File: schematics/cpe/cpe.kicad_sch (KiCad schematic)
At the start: 54 parts

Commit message: further CPE schematic updates
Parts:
- removed U24: ~, symbol peppercorn:CONFIG
- added C10, C11, C12, C13, C14, C15, C16, C17, C8, C9: ~, symbol peppercorn:MUX2B
- added FF1, FF2: ~, symbol peppercorn:DFF
- added L28: ~, symbol peppercorn:LUT2
- added L29, L30, L31, L32: ~, symbol peppercorn:LUT1
- added LT1, LT2: ~, symbol peppercorn:DLT
- added M16: ~, symbol peppercorn:MUX4 (conceptual) (upside down)
- added M17, M18, M19: ~, symbol peppercorn:MUX4
- added U24, U67, U8, U82, U83, U9: ~, symbol peppercorn:AND
- added U35, U37, U45, U80, U81, U92, U93, U96, U97, U98, U99: ~, symbol peppercorn:CONFIG
- added U77, U79, U87, U88: ~, symbol peppercorn:XOR
- added U89, U90, U91, U94, U95: ~, symbol peppercorn:NOT
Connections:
- net CINY1: now also U67., U83.
- net CLK: now also FF1.C, FF2.C, L31.D, LT1.G, LT2.G, U88.
- net COMB1OUT: now also L28.D0, M17.D0, M18.D3, U89.
- net COMB2OUT: now also L28.D1, M17.D1, M19.D3
- net EN: now also C9.D0, FF1.E, FF2.E, L30.D, LT1.E, LT2.E, U87.
- net MUXOUT: now also M17.D2, M18.D1, M19.D1, U91.
- net PINY1: now also U24., U82.
- net SR: now also C9.D1, L29.D
- net at C4.D1: now also U15.B, U19.
- net at U18.B, U21.: now also C2.D1
- net at U23.: now also U24.; no longer C3.D1
- net at U17.A: now also U79.; no longer L6.Y
- net at U17.B, U20.: now also C3.D1
- net at U22.: now also U67.; no longer C2.D1
- net at L7.Y: now also U77.; no longer U15.A
- new net: U81., U83.
- new net: U13., U5.
- new net: M19.D0, U95.
- new net: C15.Y, M19.D2
- new net: M19.S0, U98.
- new net: M19.S1, U99.
- new net: C17.D1, M19.Y, U9.
- new net: M10.D0, U27., U28.
- new net: M18.D0, U94.
- new net: C14.Y, M18.D2
- new net: M18.S0, U96.
- new net: M18.S1, U97.
- new net: C16.D1, M18.Y, U8.
- new net: M16.S0, U45.
- new net: U35., U8.
- new net: M11.S, U31., U32., U34.
- new net: U82., U87.
- new net: U80., U82.
- new net: U67., U77.
- new net: U24., U79.
- new net: C9.Y, L32.D
- new net: C8.Y, M16.D3
- new net: L30.Y, U87.
- new net: M10.S, U27., U32., U33.
- new net: U26., U27., U30.
- new net: U15.A, U77.
- new net: L31.Y, U88.
- new net: M17.D3, U91.
- new net: M17.S0, U92.
- new net: M17.S1, U93.
- new net: M17.Y, U90.
- new net: U37., U9.
- new net: C13.Y, C14.D1, C15.D0
- new net: C12.Y, C14.D0, C15.D1
- new net: L6.Y, U79.
- new net: C10.D0, FF2.Q
- new net: C10.D1, LT2.Q
- new net: C10.Y, U95.
- new net: U83., U88.
- new net: FF1.D, LT1.D, U89.
- new net: FF2.D, LT2.D, U90.
- new net: C11.D0, FF1.Q
- new net: C11.Y, U94.
- new net: C11.D1, LT1.Q
- new net COMPOUT: L28.Y
- new net COUTX: C13.D1
- new net COUTY1: C13.D0
- new net OUT1: C16.Y
- new net OUT2: C17.Y
- new net POUTX: C12.D1
- new net POUTY1: C12.D0
- new net RAM_I1: C16.D0
- new net RAM_I2: C17.D0
- new net RAM_O1: U8.
- new net RAM_O2: U9.
- new net RST: FF1.S, FF2.S, L29.Y, LT1.S, LT2.S
- new net SET: FF1.R, FF2.R, L32.Y, LT1.R, LT2.R
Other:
- sheet C_FUNCTION=0 renamed C_FUNCTION=0 or 6
- sheet C_FUNCTION=1 renamed C_FUNCTION=1 or 7
- removed sheet C_FUNCTION=6
- added sheet C_FUNCTION=2 or 3 (cpe_comb_addf2.kicad_sch)
- sheet C_FUNCTION=1 or 7: file cpe_comb_addf.kicad_sch -> cpe_comb_addcin.kicad_sch
- note added: "COMBINATIONAL LOGIC"
- note added: "C_CLKSEL"
- note added: "C_C_P"
- note added: "C_ENSEL"
- note added: "C_EN_SR"
- note added: "C_HMULT"
- note added: "C_L_D"
- note added: "C_O1[0]"
- note added: "C_O1[1]"
- note added: "C_O2[0]"
- note added: "C_O2[1]"
- note added: "C_RAMI1"
- note added: "C_RAMI2"
- note added: "C_RAM_O1"
- note added: "C_RAM_O2"
- note added: "C_S"
- note added: "C_SELX"
- note added: "C_Y12"
- note added: "D FLIP FLOP"
- note added: "D LATCH"
- note added: "SEQUENTIAL LOGIC"
- company: (none) -> YosysHQ

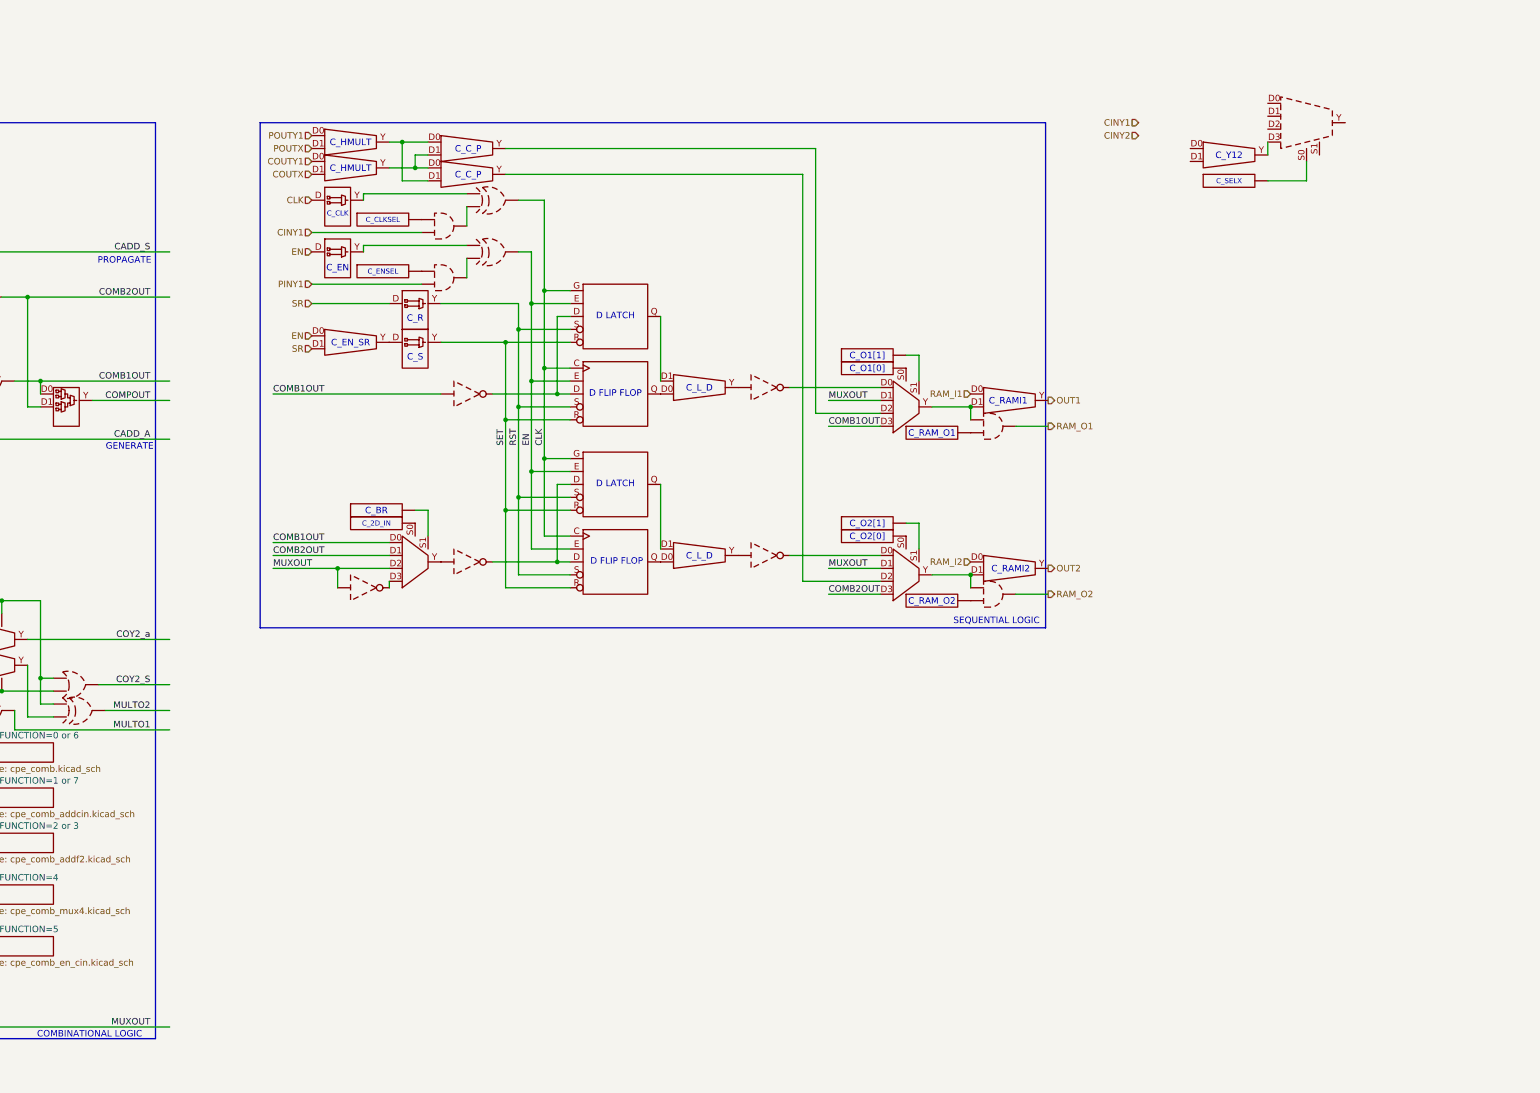
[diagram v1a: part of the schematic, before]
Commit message: update CPE schematics to cover C/P lines
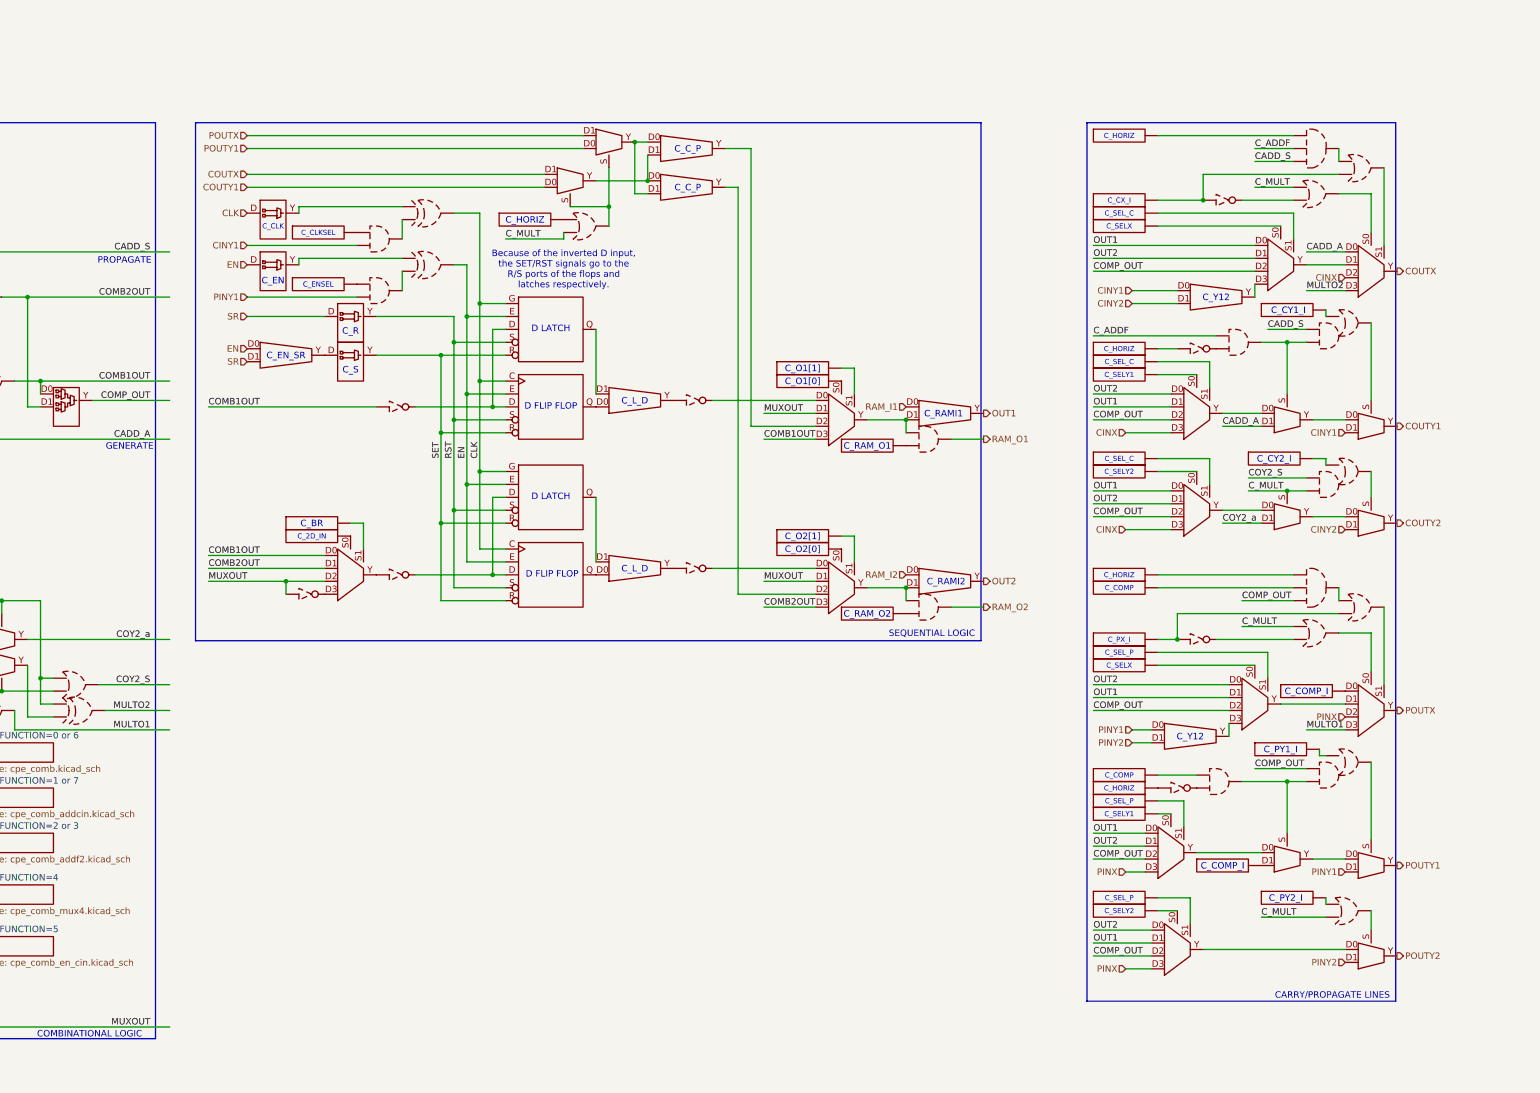
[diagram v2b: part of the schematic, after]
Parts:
- removed C13: ~, symbol peppercorn:MUX2B
- removed M16: ~, symbol peppercorn:MUX4 (conceptual) (upside down)
- added M16, M22, M27, M32, M33, M34, M37, M39: ~, symbol peppercorn:MUX4
- added M23, M24, M25, M26, M28, M29, M35, M36, M38: ~, symbol peppercorn:MUX2
- added U100, U101, U103, U107, U108, U109, U110, U111, U112, U115, U117, U119, U120, U121, U40, U51, U62, U63, U68, U69, U72, U73, U76, U78, U85, U86: ~, symbol peppercorn:CONFIG
- added U102, U105, U118, U44, U55, U60: ~, symbol peppercorn:OR
- added U104, U113, U50, U74: ~, symbol peppercorn:NOT
- added U106, U57: ~, symbol peppercorn:AND3
- added U114, U75: ~, symbol peppercorn:AND
- added U116, U70, U84: ~, symbol peppercorn:OA21
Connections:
- net CADD_A: now also M22.D0, M25.D1
- net CADD_S: now also U57., U70.
- net CINX: now also M22.D2, M27.D3, M32.D3
- net CINY1: now also C8.D0, M26.D1
- net CINY2: now also C8.D1, M29.D1
- net COUTX: now also M22.Y, M23.D1
- net COUTY1: now also M23.D0, M26.Y
- net COY2_S: now also U84.
- net COY2_a: now also M28.D1
- net MULTO1: now also M33.D3
- net MULTO2: now also M22.D3
- net OUT1: now also M16.D0, M27.D1, M32.D0, M34.D1, M37.D0, M39.D1
- net OUT2: now also M16.D1, M27.D0, M32.D1, M34.D0, M37.D1, M39.D0
- net PINX: now also M33.D2, M37.D3, M39.D3
- net PINY1: now also C12.D0, M35.D1
- net PINY2: now also C12.D1, M38.D1
- net POUTX: now also M24.D1, M33.Y; no longer C12.D1
- net POUTY1: now also M24.D0, M35.Y; no longer C12.D0
- net at U45.: now also M16.S0
- net at U77.: now also U15.A; no longer U67.
- net at U79.: now also L6.Y; no longer U24.
- net at C8.Y: now also M16.D3
- net at C14.D1, C15.D0: now also M23.Y
- net at C14.D0, C15.D1: now also M24.Y; no longer C12.Y
- net COMPOUT renamed COMP_OUT
- net COMP_OUT: now also M16.D2, M27.D2, M32.D2, M34.D2, M37.D2, M39.D2, U106., U116.
- new net: M33.D0, U86.
- new net: U13., U5.
- new net: M37.S0, U112.
- new net: M28.Y, M29.D0
- new net: M29.S, U84.
- new net: M10.D0, U27., U28.
- new net: U106., U107.
- new net: U118., U119.
- new net: M38.S, U118.
- new net: U84., U85.
- new net: U103., U104., U105.
- new net: U102., U104.
- new net: M23.S, M24.S, U60.
- new net: M36.S, U114., U116.
- new net: U114., U115.
- new net: U113., U114.
- new net: M16.S1, U40.
- new net: M28.D0, M32.Y
- new net: M27.S1, U68.
- new net: M34.S0, U101.
- new net: M25.S, U70., U75.
- new net: U74., U75.
- new net: M33.S1, U105.
- new net: U105., U106.
- new net: M11.S, U31., U32., U34.
- new net: U82., U87.
- new net: U67., U77.
- new net: M39.S1, U120.
- new net: U44., U50.
- new net: M22.S0, U44.
- new net: U110., U113.
- new net: U24., U79.
- new net: M38.D0, M39.Y
- new net: U60., U63.
- new net: M26.S, U70.
- new net: U70., U72.
- new net: M36.D1, U109.
- new net: M10.S, U27., U32., U33.
- new net: U26., U27., U30.
- new net: U73., U74.
- new net: M32.S0, U78.
- new net: M32.S1, U76.
- new net: M33.D1, M34.Y
- new net: M33.S0, U102.
- new net: U116., U117.
- new net: M35.S, U116.
- new net: M37.S1, U111.
- new net: M36.D0, M37.Y
- new net: M34.S1, U100.
- new net: M39.S0, U121.
- new net: U50., U51., U55.
- new net: U57., U62.
- new net: M16.Y, M22.D1
- new net: C12.Y, M34.D3
- new net: M35.D0, M36.Y
- new net: M22.S1, U55.
- new net: M27.S0, U69.
- new net: M25.D0, M27.Y
- new net: U83., U88.
- new net: M25.Y, M26.D0
- new net: U106., U108.
- new net: U55., U57.
- new net COUTY2: M29.Y
- new net C_ADDF: U57., U75.
- new net C_MULT: M28.S, U102., U118., U44., U60., U84.
- new net POUTY2: M38.Y
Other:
- note added: "Because of the inverted D input, the SET/RST signals go to the R/S ports of the flops and latches respectively."
- note added: "CARRY/PROPAGATE LINES"
- note added: "C_COMP"
- note added: "C_COMP_I"
- note added: "C_CX_I"
- note added: "C_CY1_I"
- note added: "C_CY2_I"
- note added: "C_PX_I"
- note added: "C_PY1_I"
- note added: "C_PY2_I"
- note added: "C_SELY1"
- note added: "C_SELY2"
- note added: "C_SEL_C"
- note added: "C_SEL_P"
- note removed: "C_HMULT"

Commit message: update schematics to include switchboxes
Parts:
- added L21: ~, symbol peppercorn:LUT2
- added L22: ~, symbol peppercorn:LUT2 with C_I mux
- added U122: ~, symbol peppercorn:MUX invert/mask
- renumbered C1 to C156, C2 to C157, C3 to C158, C4 to C159, C9 to C160, C11 to C161, C10 to C162, C14 to C163, C15 to C164, C16 to C165, C17 to C166, C8 to C168, C_FUNCTION to C_FUNCTION11, FF1 to FF21, FF2 to FF22, INIT_L01 to INIT_L151, INIT_L02 to INIT_L152, INIT_L03 to INIT_L153, L5 to L290, L6 to L291, L7 to L292, L1 to L293, L3 to L294, L2 to L295, L4 to L296, L28 to L297, L32 to L301, LT1 to LT21, LT2 to LT22, M1 to M514, M2 to M515, M7 to M516, M9 to M517, M3 to M518, M4 to M519, M6 to M520, M5 to M521, M8 to M522, M10 to M523, M11 to M524, M17 to M525, M23 to M526, M24 to M527, M18 to M528, M19 to M529, M37 to M530, M39 to M531, M27 to M532, M32 to M533, M34 to M534, M16 to M535, M25 to M536, M28 to M537, M36 to M538, M22 to M539, M26 to M540, M29 to M541, M33 to M542, M35 to M543, M38 to M544, U21 to U1343, U20 to U1344, U19 to U1345, U14 to U1346, U4 to U1347, U1 to U1350, U28 to U1351, U29 to U1352, U12 to U1357, U16 to U1358, U25 to U1359, U18 to U1360, U17 to U1361, U15 to U1362, U2 to U1363, U3 to U1364, U31 to U1365, U30 to U1366, U13 to U1367, U26 to U1368, U27 to U1369, U5 to U1370, U34 to U1371, U32 to U1372, U33 to U1373, U91 to U1374, U93 to U1375, U92 to U1376, U89 to U1381, U90 to U1382, U63 to U1385, U60 to U1387, U94 to U1388, U95 to U1389, U97 to U1390, U96 to U1391, U99 to U1392, U98 to U1393, U35 to U1394, U37 to U1395, U8 to U1396, U9 to U1397, U62 to U1398, U51 to U1399, U45 to U1401, U74 to U1419, U104 to U1420, U50 to U1422, U75 to U1424, U85 to U1425, U117 to U1426, U72 to U1427, U119 to U1428, U86 to U1429, U57 to U1430, U106 to U1431, U44 to U1432, U102 to U1433, U70 to U1434, U84 to U1435, U116 to U1436, U118 to U1437, U55 to U1438, U105 to U1439
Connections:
- net at U1419.: now also U73.; no longer U1424.
- net at U77.: now also U1362.A; no longer U67.
- net at U1422.: now also U1399., U1438.; no longer U1432.
- net at U79.: now also L291.Y; no longer U24.
- new net: U1367., U1370.
- new net: M523.D0, U1351., U1369.
- new net: U103., U1420., U1439.
- new net: M538.S, U114., U1436.
- new net: M536.S, U1424., U1434.
- new net: U1419., U1424.
- new net: M524.S, U1365., U1371., U1372.
- new net: U82., U87.
- new net: U67., U77.
- new net: U1422., U1432.
- new net: U24., U79.
- new net: M523.S, U1369., U1372., U1373.
- new net: U1366., U1368., U1369.
- new net: U83., U88.
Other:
- note added: "LUT2"
- note added: "LUT2 WITH C_I MUX"
- note added: "MUX4 INPUT INVERSION AND MASKING"
- note added: "SYMBOL LEGEND"

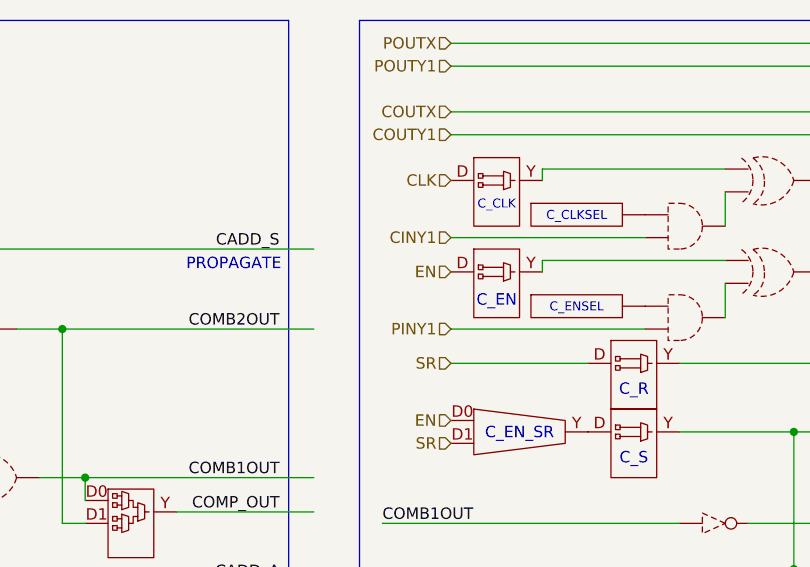
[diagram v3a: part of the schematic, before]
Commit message: fix C_CLKSEL/C_ENSEL input
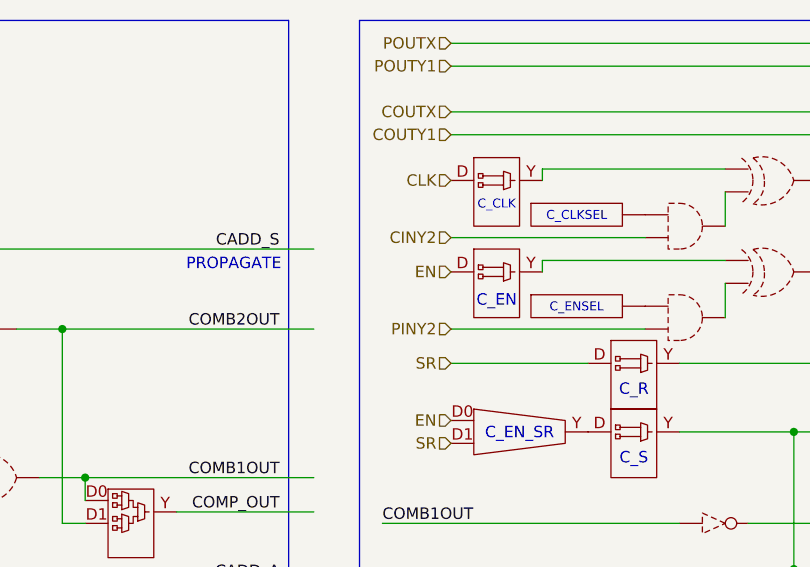
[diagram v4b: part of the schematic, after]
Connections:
- net CINY1: no longer U83.
- net CINY2: now also U83.
- net PINY1: no longer U82.
- net PINY2: now also U82.
- net at U1419.: now also U73.; no longer U1424.
- net at U77.: now also U1362.A; no longer U67.
- net at U1422.: now also U1399., U1438.; no longer U1432.
- net at U79.: now also L291.Y; no longer U24.
- new net: U1367., U1370.
- new net: M523.D0, U1351., U1369.
- new net: U103., U1420., U1439.
- new net: M538.S, U114., U1436.
- new net: M536.S, U1424., U1434.
- new net: U1419., U1424.
- new net: M524.S, U1365., U1371., U1372.
- new net: U82., U87.
- new net: U67., U77.
- new net: U1422., U1432.
- new net: U24., U79.
- new net: M523.S, U1369., U1372., U1373.
- new net: U1366., U1368., U1369.
- new net: U83., U88.
